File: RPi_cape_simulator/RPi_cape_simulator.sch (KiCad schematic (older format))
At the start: 57 parts, among them J1 Conn_01x12, J15 Conn_01x06, J16 Conn_01x06, J2 Conn_02x20_Odd_Even, J21 Conn_01x06, J3 Conn_01x12, J5 Conn_02x20_Odd_Even, J8 Conn_02x20_Odd_Even, Q1 DNP, Q2 DNP, Q3 DNP, Q4 DNP

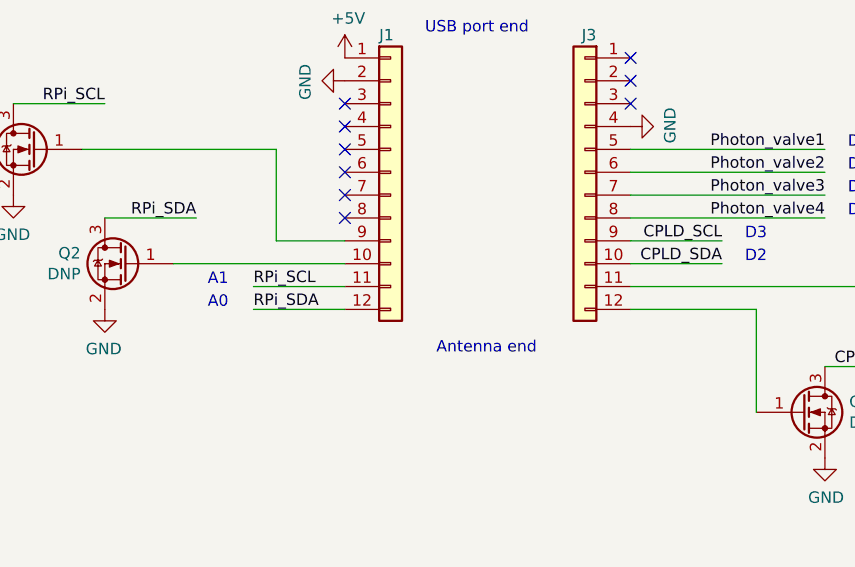
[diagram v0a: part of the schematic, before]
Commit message: Misc small updates
Updated non-precision op-amp list to work with valve-motion-detect circuit's peak detector (needs low bias current)
Created 3D model for "quick and dirty" prototype board
Added rework on simulator for Photon pinout
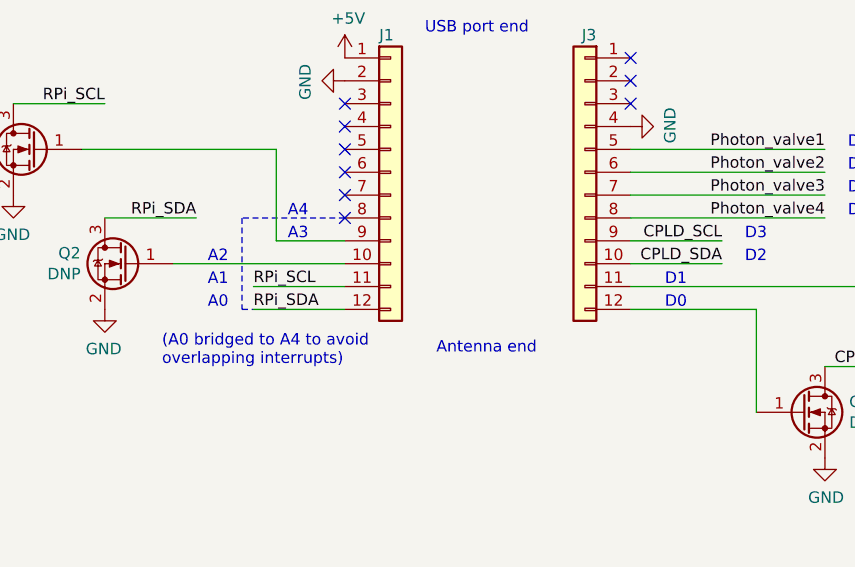
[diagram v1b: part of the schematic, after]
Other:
- note added: "(A0 bridged to A4 to avoid\noverlapping interrupts)"
- note added: "A2"
- note added: "A3"
- note added: "A4"
- note added: "D0"
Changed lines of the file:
@@
 Title "GlobalVent Controller: Software Simulator"
 Date ""
-Rev "1.0"
+Rev "1.0r1"
 Comp "US GlobalVent Team"
 Comment1 "Licensed under CERN-OHL-S v2"
@@
 Wire Wire Line
 	4300 5200 4700 5200
+Text Notes 5150 5900 0    50   ~ 0
+A2
+Text Notes 5500 5800 0    50   ~ 0
+A3
+Text Notes 7150 6100 0    50   ~ 0
+D0
+Text Notes 7150 6000 0    50   ~ 0
+D1
+Wire Notes Line
+	5750 5700 5300 5700
+Wire Notes Line
+	5300 5700 5300 6100
+Wire Notes Line
+	5300 6100 5350 6100
+Text Notes 4950 6350 0    50   ~ 0
+(A0 bridged to A4 to avoid\noverlapping interrupts)
+Text Notes 5500 5700 0    50   ~ 0
+A4
 $EndSCHEMATC
